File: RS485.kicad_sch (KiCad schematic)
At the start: 7 parts

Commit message: 回路図の作成
完成が見えてきた
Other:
- note added: "RS485_Flag"
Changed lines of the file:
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@@
 	(paper "A4")
+	(rectangle
+		(start 135.89 19.05)
+		(end 153.67 30.48)
+		(stroke
+			(width 0)
+			(type default)
+		)
+		(fill
+			(type none)
+		)
+	)
 	(rectangle
 		(start 15.24 19.05)
@@
 		(fill
 			(type none)
+		)
+	)
+	(text "RS485_Flag"
+		(exclude_from_sim no)
+		(at 135.89 17.78 0)
+		(effects
+			(font
+				(size 1.27 1.27)
+				(thickness 0.1588)
+				(color 0 0 0 1)
+			)
+			(justify left)
 		)
 	)
@@
 	(wire
 		(pts
+			(xy 137.16 25.4) (xy 144.78 25.4)
+		)
+		(stroke
+			(width 0)
+			(type default)
+		)
+	)
+	(wire
+		(pts
 			(xy 69.85 26.67) (xy 71.12 26.67)
 		)
@@
 		(pts
 			(xy 63.5 29.21) (xy 71.12 29.21)
+		)
+		(stroke
+			(width 0)
+			(type default)
+		)
+	)
+	(wire
+		(pts
+			(xy 137.16 27.94) (xy 144.78 27.94)
+		)
+		(stroke
+			(width 0)
+			(type default)
+		)
+	)
+	(wire
+		(pts
+			(xy 137.16 22.86) (xy 144.78 22.86)
 		)
 		(stroke
@@
 		)
 	)
+	(label "UARTTX"
+		(at 137.16 22.86 0)
+		(effects
+			(font
+				(size 1.27 1.27)
+			)
+			(justify left bottom)
+		)
+	)
 	(label "RS485_A"
 		(at 63.5 52.07 0)
@@
 		)
 	)
+	(label "URTRX"
+		(at 137.16 25.4 0)
+		(effects
+			(font
+				(size 1.27 1.27)
+			)
+			(justify left bottom)
+		)
+	)
 	(label "CTRL"
 		(at 17.78 41.91 0)
@@
 		)
 	)
+	(label "CTRL"
+		(at 137.16 27.94 0)
+		(effects
+			(font
+				(size 1.27 1.27)
+			)
+			(justify left bottom)
+		)
+	)
+	(hierarchical_label "CTRL"
+		(shape input)
+		(at 144.78 27.94 0)
+		(effects
+			(font
+				(size 1.27 1.27)
+			)
+			(justify left)
+		)
+	)
+	(hierarchical_label "UARTRX"
+		(shape input)
+		(at 144.78 25.4 0)
+		(effects
+			(font
+				(size 1.27 1.27)
+			)
+			(justify left)
+		)
+	)
+	(hierarchical_label "UARTTX"
+		(shape input)
+		(at 144.78 22.86 0)
+		(effects
+			(font
+				(size 1.27 1.27)
+			)
+			(justify left)
+		)
+	)

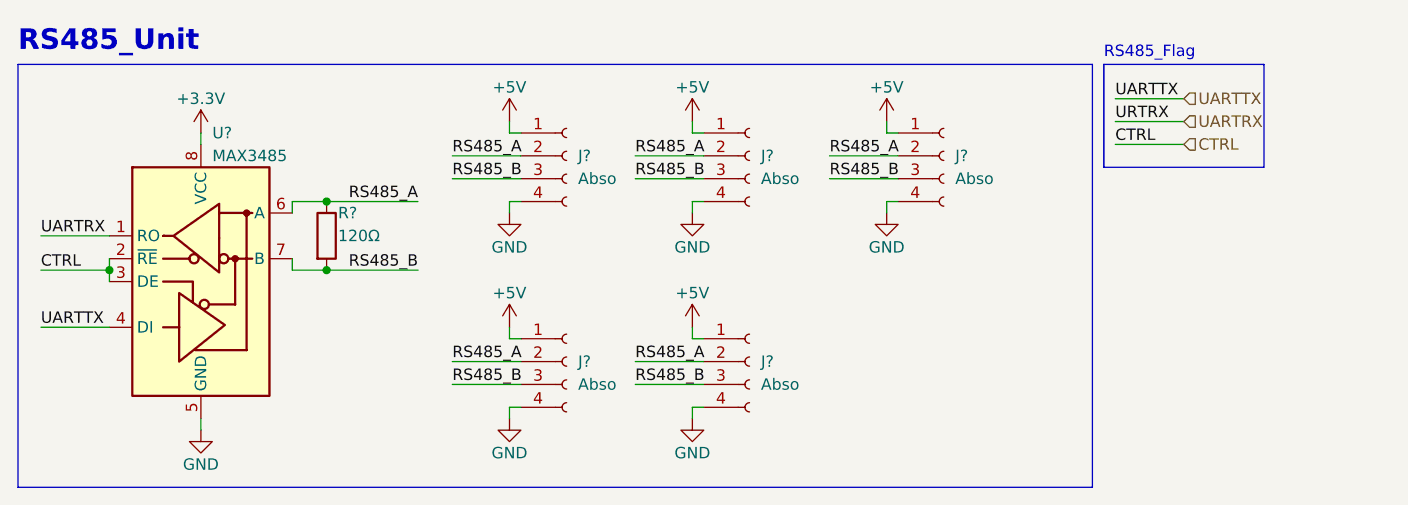
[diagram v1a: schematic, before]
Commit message: 回路図9割完成
回路図は9割完成
次からは配線作業をする
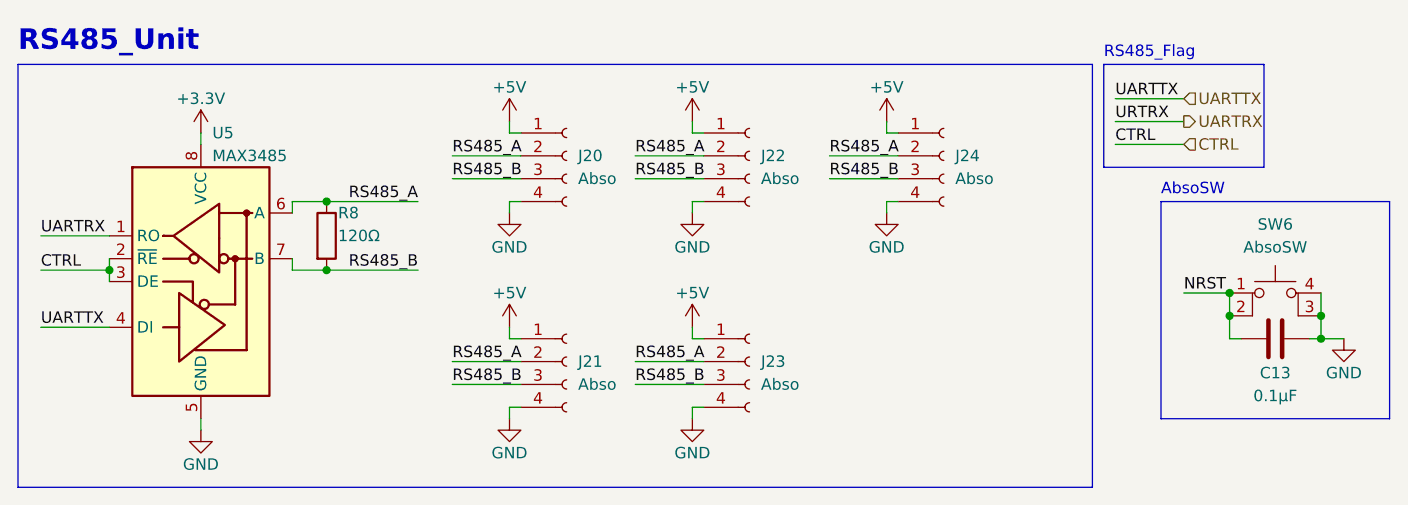
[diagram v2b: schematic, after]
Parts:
- added C13: 0.1μF, Capacitor_SMD:C_0603_1608Metric, symbol Device:C
- added SW6: AbsoSW, symbol Switch:SW_MEC_5E
- R8: renamed from R?; footprint (none) -> Resistor_SMD:R_0603_1608Metric
- gave numbers to parts that had none: 6
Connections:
- net GND: now also C13.1, SW6.3 (K), SW6.4 (A)
- new net NRST: C13.2, SW6.1, SW6.2
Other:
- note added: "AbsoSW"

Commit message: 回路図作った
リミットとエンコ共存いやかも
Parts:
- removed C13: 0.1μF, Capacitor_SMD:C_0603_1608Metric, symbol Device:C
- removed J20, J21, J22, J23, J24: Abso, Connector_JST:JST_XA_S04B-XASK-1_1x04_P2.50mm_Horizontal, symbol Connector:Conn_01x04_Socket
- removed R8: 120Ω, Resistor_SMD:R_0603_1608Metric, symbol Device:R
- removed SW6: AbsoSW, symbol Switch:SW_MEC_5E
- removed U5: MAX3485, Package_SO:SOIC-8_3.9x4.9mm_P1.27mm, symbol Interface_UART:MAX3485
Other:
- note removed: "AbsoSW"
- note removed: "RS485_Unit"
